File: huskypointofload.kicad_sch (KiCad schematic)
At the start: 12 parts, among them J1 POWER, J2 RFSOC_POWER, J39 10MHZ, U18 ADA4077-1xR, U27 ADL8124, U28 LT3093xMSE

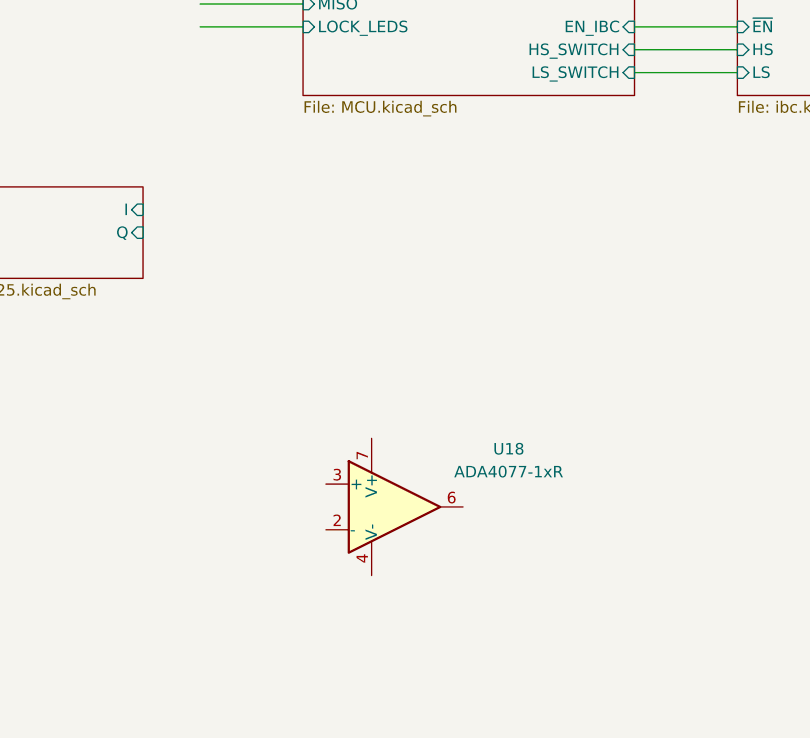
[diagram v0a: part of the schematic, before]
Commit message: Add VVA Bias generator
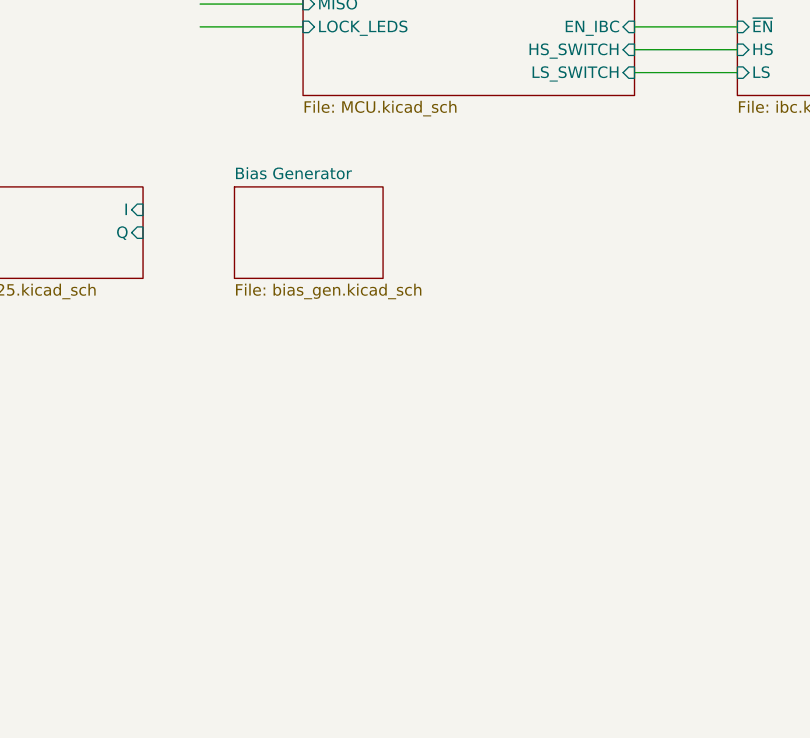
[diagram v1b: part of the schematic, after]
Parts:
- removed U18: ADA4077-1xR, Package_SO:SOIC-8_3.9x4.9mm_P1.27mm, symbol Amplifier_Operational:ADA4077-1xR
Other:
- added sheet Bias Generator (bias_gen.kicad_sch)
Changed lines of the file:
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@@
-		)
-	)
-	(symbol
-		(lib_id "Amplifier_Operational:ADA4077-1xR")
-		(at 231.14 119.38 0)
-		(unit 1)
-		(exclude_from_sim no)
-		(in_bom yes)
-		(on_board yes)
-		(dnp no)
-		(fields_autoplaced yes)
-		(property "Reference" "U18"
-			(at 243.84 112.9598 0)
-			(effects
-				(font
-					(size 1.27 1.27)
-				)
-			)
-		)
-		(property "Value" "ADA4077-1xR"
-			(at 243.84 115.4998 0)
-			(effects
-				(font
-					(size 1.27 1.27)
-				)
-			)
-		)
-		(property "Footprint" "Package_SO:SOIC-8_3.9x4.9mm_P1.27mm"
-			(at 228.6 124.46 0)
-			(effects
-				(font
-					(size 1.27 1.27)
-				)
-				(justify left)
-				(hide yes)
-			)
-		)
-		(property "Datasheet" "https://www.analog.com/media/en/technical-documentation/data-sheets/ADA4077-1_4077-2_4077-4.pdf"
-			(at 234.95 115.57 0)
-			(effects
-				(font
-					(size 1.27 1.27)
-				)
-				(hide yes)
-			)
-		)
-		(property "Description" "4MHz, 7nV/sqrtHz, Low Offset and Drift, High Precision Amplifier, SOIC-8"
-			(at 231.14 119.38 0)
-			(effects
-				(font
-					(size 1.27 1.27)
-				)
-				(hide yes)
-			)
-		)
-		(pin "6"
-		)
-		(pin "1"
-		)
-		(pin "5"
-		)
-		(pin "4"
-		)
-		(pin "3"
-		)
-		(pin "8"
-		)
-		(pin "7"
-		)
-		(pin "2"
-		)
-		(instances
-			(project ""
-				(path "/eb9c972b-d134-41da-be97-ece3f463f7e0"
-					(reference "U18")
-					(unit 1)
-				)
-			)
 		)
 	)
@@
 				)
 			)
+		)
+	)
+	(sheet
+		(at 213.36 83.82)
+		(size 16.51 10.16)
+		(exclude_from_sim no)
+		(in_bom yes)
+		(on_board yes)
+		(dnp no)
+		(fields_autoplaced yes)
+		(stroke
+			(width 0.1524)
+			(type solid)
+		)
+		(fill
+			(color 0 0 0 0.0000)
+		)
+		(property "Sheetname" "Bias Generator"
+			(at 213.36 83.1084 0)
+			(effects
+				(font
+					(size 1.27 1.27)
+				)
+				(justify left bottom)
+			)
+		)
+		(property "Sheetfile" "bias_gen.kicad_sch"
+			(at 213.36 94.5646 0)
+			(effects
+				(font
+					(size 1.27 1.27)
+				)
+				(justify left top)
+			)
+		)
+		(instances
+			(project "huskypointofload"
+				(path "/eb9c972b-d134-41da-be97-ece3f463f7e0"
+					(page "22")
+				)
+			)
